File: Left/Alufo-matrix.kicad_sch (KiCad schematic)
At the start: 41 parts, among them K11 PG1350, K12 PG1350, K13 PG1350, K14 PG1350, K15 PG1350, K16 PG1350, K21 PG1350, K22 PG1350, K23 PG1350, K24 PG1350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

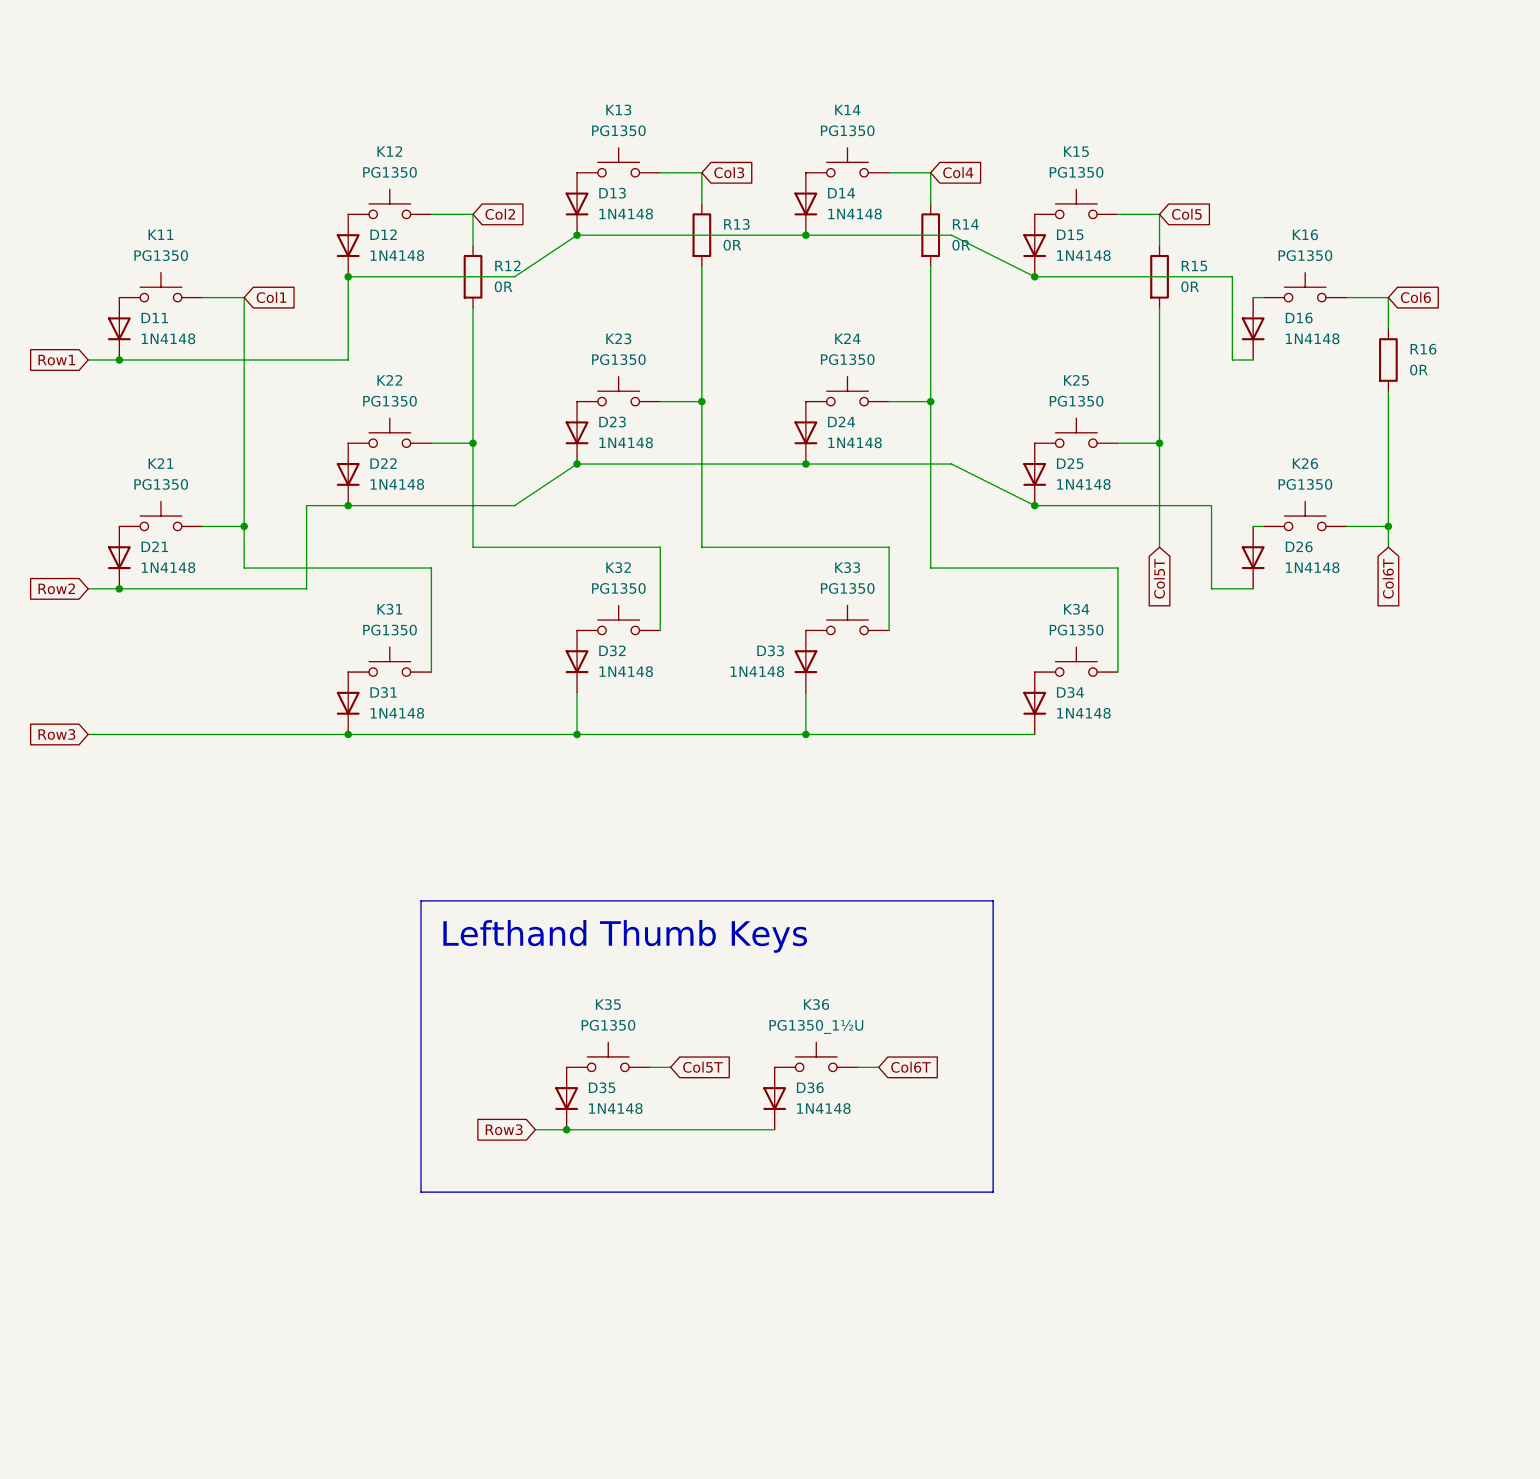
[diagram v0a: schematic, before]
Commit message: Add lefthand plate
The plate file is arranged to the left of the main PCB. This arrangement is a little more costly  than if the plate were upside down under the PCB. However, the cost difference is small (~$3 for a five-PCB run) and this way makes it easier to crosscheck and make matching adjustments to the plate and the PCB.
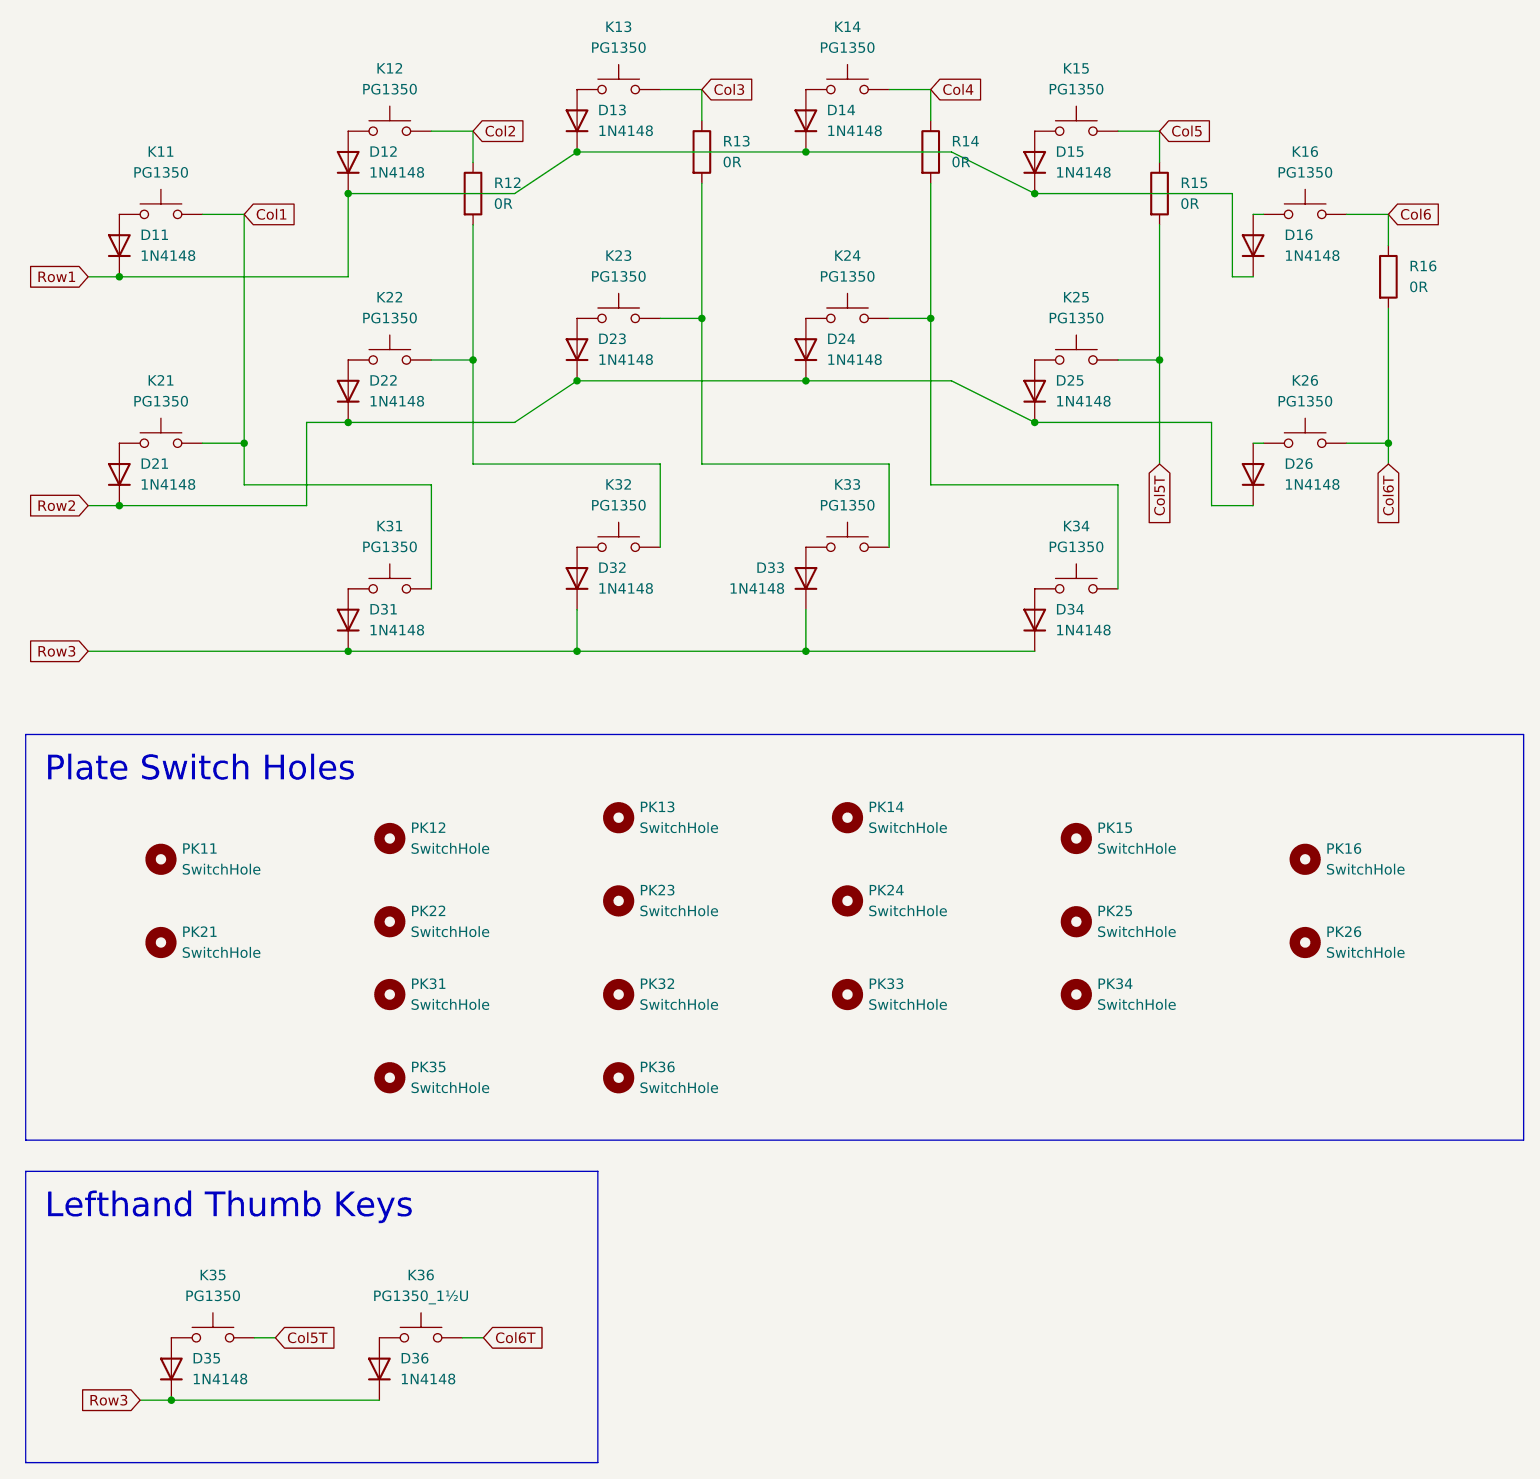
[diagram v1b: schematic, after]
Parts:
- added PK11, PK12, PK13, PK14, PK15, PK16, PK21, PK22, PK23, PK24, PK25, PK26, PK31, PK32, PK33, PK34, PK35: SwitchHole, Project Library:SW_choc_v1_Plate_CPG135001S30_1u, symbol Mechanical:MountingHole
- added PK36: SwitchHole, Project Library:SW_choc_v1_Plate_CPG135001S30_1.5u, symbol Mechanical:MountingHole
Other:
- moved on the sheet: D11, D12, D13, D14, D15, D16, D21, D22, D23, D24, D25, D26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
